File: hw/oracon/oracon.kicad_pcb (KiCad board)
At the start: 4 copper layers, 81 x 56 mm, 108 parts, among them J2 SIM_Card, J3 USB_A, J4 Conn_Coaxial, J5 USB_C_Receptacle_USB2.0_16P, Q1 SS8050, Q2 SS8050, Q3 SS8050, Q5 SS8050, SW1 SW_Push, U1 TP5100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

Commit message: finishing before ordering
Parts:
- J2: value SIM_Card -> SIM_Holder
- TP4: value SW4 -> SW2
- renumbered SW1 to SW3
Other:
- board text added: "ANT"
- board text added: "BAT"
- board text added: "RS232"
- board text added: "SW1"
- board text added: "SW2"

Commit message: CSQ fix, hw work, cleanup
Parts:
- removed Q5: SS8050, Package_TO_SOT_SMD:SOT-23
- removed R33: 4,7K, Resistor_SMD:R_0402_1005Metric
- removed R34: 47K, Resistor_SMD:R_0402_1005Metric
- C23: value C -> 104
- C27, C28: value C -> DNP
- J3: moved to F.Cu
- R3: value 0R1 -> 120mR
- R31, R32: value R -> 0R
- R4, R6: value x -> DNP
- moved C31 1.33 mm to (22.6, 54.7)
- moved SW3 1.20 mm to (26.8, 55.0), turned to 0 degrees
- moved R13 0.27 mm to (16.1, 93.8)
- moved J3 0.08 mm to (39.3, 69.2), turned to 90 degrees
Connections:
- C31 pad 1: Net-(Q5-C) -> NB_RST
- SW3 pad 1: Net-(Q5-C) -> NB_RST
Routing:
- net Net-(Q5-C): track 8.14 -> 0.00 mm, vias 1 -> 0
- net Net-(Q5-B): track 3.88 -> 0.00 mm
- net NB_RST: track 40.7 -> 43.4 mm, vias 1 -> 2
- net GND: track 88.2 -> 87.1 mm

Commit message: To be checked for production.
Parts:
- removed TP1: BATT, TestPoint:TestPoint_Pad_D1.5mm
- removed TP2: GND, TestPoint:TestPoint_Pad_D1.5mm
- added J6: Conn_01x02_MountingPin, kolskypavel:CONN-TH_B2B-PH-K-S, B.Cu at (42.5, 95.2)
- R10, R11: moved to F.Cu
- moved R11 5.49 mm to (7.89, 100.4), turned to -90 degrees
- moved TP4 4.54 mm to (20.2, 90.8)
- moved Q3 4.52 mm to (20.6, 61.5), turned to 0 degrees
- moved C23 4.43 mm to (-2.26, 87.4)
- moved C36 3.72 mm to (-2.56, 79.8), turned to 0 degrees
- moved R10 3.53 mm to (6.88, 100.4), turned to 90 degrees
- moved D6 3.21 mm to (18.9, 57.4)
- moved C31 3.08 mm to (22.9, 57.8)
- moved R27 3.08 mm to (21.8, 57.8)
- moved H4 2.96 mm to (41.2, 101.2)
- moved R12 2.89 mm to (17.4, 60.8)
- moved R26 2.89 mm to (17.4, 61.8)
- moved J2 2.83 mm to (-5.03, 95.1)
- moved SW3 2.75 mm to (27.3, 57.7)
- moved C4 2.62 mm to (37.5, 96.1), turned to 0 degrees
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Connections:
- U3 pad 23: unconnected-(U3-IO19-Pad23) -> USB_SI_N
- U3 pad 24: unconnected-(U3-IO20-Pad24) -> USB_SI_P
- U3 pad 7: USB_SI_N -> unconnected-(U3-IO3-Pad7)
- U3 pad 8: USB_SI_P -> unconnected-(U3-IO4-Pad8)
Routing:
- net USB_SI_P: track 41.6 -> 73.6 mm, vias 2 -> 0
- net USB_SI_N: track 41.5 -> 71.3 mm, vias 2 -> 0
- net +5V: track 62.5 -> 37.5 mm
- net VCC: track 41.0 -> 23.5 mm
- net GND: track 87.1 -> 72.3 mm, vias 161 -> 126
- net VBUS: track 165.0 -> 155.8 mm, vias 4 -> 7
- net NBIOT_RX: track 44.0 -> 37.2 mm
- net NBIOT_TX: track 42.9 -> 36.4 mm
- net NB_RST: track 43.4 -> 37.0 mm, vias 2 -> 1
- net NETLIGHT: track 30.2 -> 24.9 mm
- net ADC_BATT: track 3.26 -> 8.30 mm, vias 0 -> 1
- net SIM_VDD: track 41.9 -> 37.4 mm
- net CHG_STAT: track 71.6 -> 67.4 mm, vias 3 -> 4
- net +3.3V: track 190.5 -> 194.6 mm, vias 11 -> 9
- net +BATT: track 18.2 -> 21.3 mm
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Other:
- board size 81 x 56 mm -> 81 x 50 mm

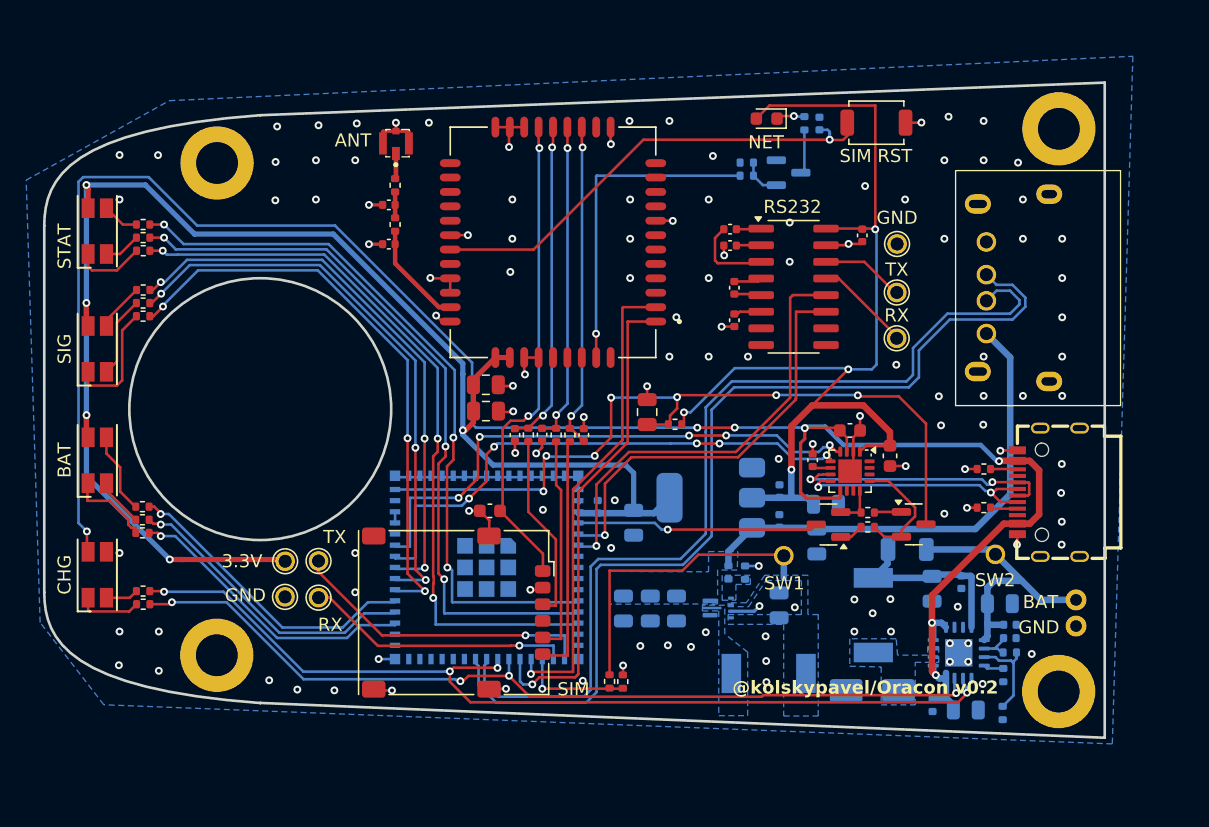
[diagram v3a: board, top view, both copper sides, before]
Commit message: added connectors, USB + dimensions to be checked
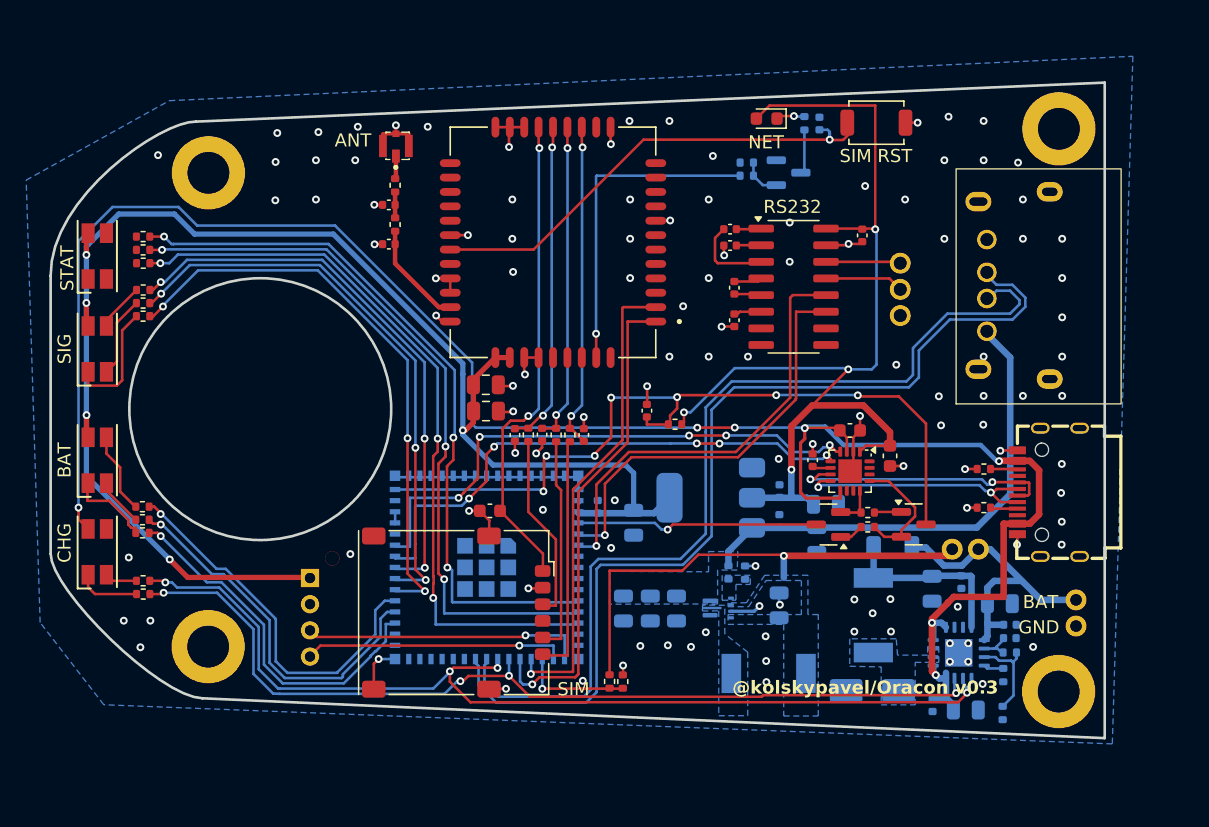
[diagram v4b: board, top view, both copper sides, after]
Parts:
- removed C14: 10u, Capacitor_SMD:C_0805_2012Metric
- removed H5: SI_TX, TestPoint:TestPoint_Pad_D1.5mm
- removed H6: SI_RX, TestPoint:TestPoint_Pad_D1.5mm
- removed H7: SI_GND, TestPoint:TestPoint_Pad_D1.5mm
- removed H8: SI_3.3V, TestPoint:TestPoint_Pad_D1.5mm
- removed TP3: SW1, TestPoint:TestPoint_Pad_D1.5mm
- removed TP4: SW2, TestPoint:TestPoint_Pad_D1.5mm
- removed TP5: Serial_TX, TestPoint:TestPoint_Pad_D1.5mm
- removed TP6: Serial_RX, TestPoint:TestPoint_Pad_D1.5mm
- removed TP7: Serial_GND, TestPoint:TestPoint_Pad_D1.5mm
- added C29: 100n, Capacitor_SMD:C_0402_1005Metric, F.Cu at (9.73, 79.7)
- added CN1: B3B-PH-K-S, kolskypavel:CONN-TH_B3B-PH-K-S, B.Cu at (29.1, 70.5)
- added J1: Conn_01x02_MountingPin, kolskypavel:CONN-TH_B2B-PH-K-S, B.Cu at (34.1, 90.3)
- added U8: B4B-XH-A, kolskypavel:CONN-TH_B04B-PASK-1-LF-SN, B.Cu at (-16.0, 95.5)
- moved J3 11.3 mm to (33.4, 79.2)
- moved D2 1.91 mm to (-32.2, 67.9)
- moved D5 1.75 mm to (-32.2, 90.5)
- moved R3 1.11 mm to (28.5, 90.2)
- moved H1 1.00 mm to (-23.8, 61.5)
- moved R15 0.95 mm to (-28.7, 68.5)
- moved R16 0.94 mm to (-28.8, 67.4)
- moved H3 0.93 mm to (-23.8, 97.7)
- moved R17 0.92 mm to (-28.8, 66.4)
- moved R25 0.79 mm to (-28.8, 92.7)
- moved R24 0.77 mm to (-28.7, 93.7)
- moved J4 0.20 mm to (-9.44, 59.4)
- moved C8 0.11 mm to (22.7, 89.6)
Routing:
- net VCC: track 23.5 -> 36.2 mm, vias 0 -> 1
- net LED3_B: track 23.5 -> 29.4 mm
- net LED3_G: track 23.0 -> 28.7 mm
- net LED3_R: track 22.6 -> 28.0 mm
- net Net-(D2-RK): track 5.40 -> 0.00 mm
- net VBUS: track 155.8 -> 151.6 mm
- net STBY_STAT: track 72.3 -> 75.6 mm
- net CHG_STAT: track 67.4 -> 70.5 mm
- net Net-(D2-GK): track 2.81 -> 0.00 mm
- net Net-(D2-BK): track 2.81 -> 0.00 mm
- net +3.3V: track 194.6 -> 191.9 mm
- net +BATT: track 21.3 -> 23.5 mm
- net SI_TX: track 23.5 -> 21.6 mm
- net GND: track 72.3 -> 70.9 mm, vias 126 -> 117
- net Net-(U6-R1IN): track 6.76 -> 6.02 mm
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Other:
- board size 81 x 50 mm -> 80.5 x 50.1 mm
- board text added: "@kolskypavel/Oracon v0.3"
- board text added: "SRR"
- board text added: "SW"
- board text removed: "3.3V"
- board text removed: "@kolskypavel/Oracon v0.2"
- board text removed: "RX"
- board text removed: "SW1"
- board text removed: "SW2"
- board text removed: "TX"

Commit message: usb position modifications
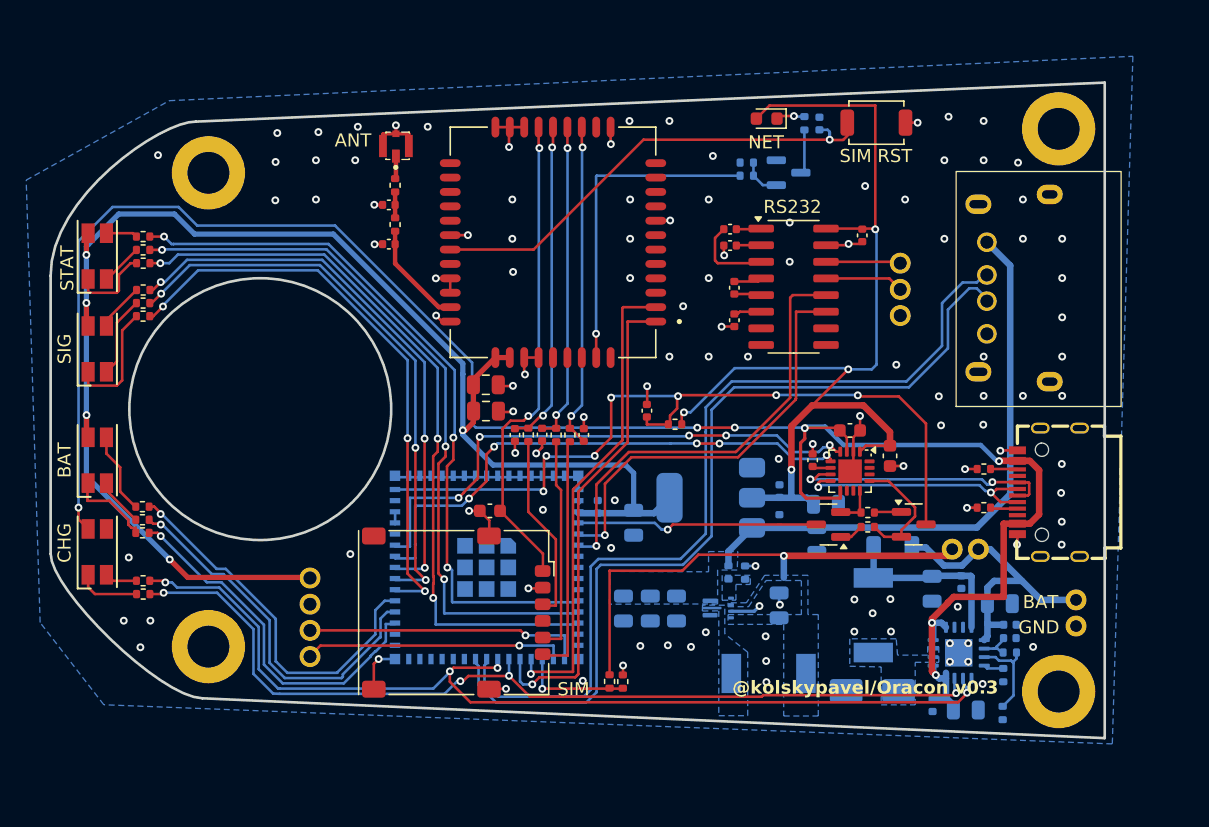
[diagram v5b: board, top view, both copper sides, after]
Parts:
- U8: value B4B-XH-A -> B4B-PH-K-S; footprint kolskypavel:CONN-TH_B04B-PASK-1-LF-SN -> kolskypavel:CONN-TH_B4B-PH-K-S
- moved J3 0.20 mm to (33.4, 79.3)
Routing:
- net +5V: track 37.2 -> 44.2 mm
- net Net-(D2-RK): track 0.00 -> 6.34 mm
- net USB_SI_P: track 73.6 -> 67.7 mm
- net USB_SI_N: track 71.3 -> 67.1 mm
- net Net-(D2-GK): track 0.00 -> 3.21 mm
- net Net-(D2-BK): track 0.00 -> 2.40 mm
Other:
- board text added: "SERIAL"
